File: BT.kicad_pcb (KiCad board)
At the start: 4 copper layers, 55 x 40 mm, 77 parts, among them J1 Conn_01x06_Pin, J2 Conn_01x05_Pin, J3 Conn_01x03_Pin, K1 AGQ200S12Z, Q1 BSS123, U1 ESP32-WROOM-32U, U2 AMS1117-3.3, U3 AP64060WU-7, U5 TPS7A4701, U6 PCM5100A, U7 CP2102N-A02-GQFN28, Y1 XO32

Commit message: rough placement
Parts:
- removed the C10 at (185.7, 102.7)
- removed the C25 at (205.3, 84.4)
- removed the C26 at (205.3, 86.9)
- removed the C9 at (185.7, 105.2)
- removed the R1 at (179.2, 79.2)
- removed R11, R24: 10K, NRD_RES:R_0603
- removed the R15 at (192.7, 89.7)
- removed the R16 at (192.7, 87.2)
- removed the R17 at (192.7, 84.7)
- removed the R2 at (183.4, 79.0)
- removed R21: 22K1, NRD_RES:R_0603
- removed R22: 47K5, NRD_RES:R_0603
- removed R23: 1K, NRD_RES:R_0603
- removed the R4 at (183.4, 76.5)
- removed the R5 at (179.2, 76.7)
- removed the R7 at (192.2, 78.7)
- removed the R7 at (184.7, 96.2)
- removed U7: CP2102N-A02-GQFN28, NRD_IC_COM:CP2102N
- added J5: Conn_02x03_Odd_Even, Connector_PinHeader_1.27mm:PinHeader_2x03_P1.27mm_Vertical_SMD, F.Cu at (144.6, 106.6)
- added R3: 10K, NRD_RES:R_0603, F.Cu at (131.6, 114.2)
- added R7: 10K, NRD_RES:R_0603, F.Cu at (138.4, 114.2)
- R6: renamed from R8; value 22K1 -> 1K
- R8: value 22K1 -> 10K
- moved R16 71.2 mm to (121.8, 88.3), turned to 90 degrees
- moved Y1 68.0 mm to (122.6, 91.7), turned to 0 degrees
- moved C5 65.5 mm to (122.3, 114.1)
- moved C16 64.7 mm to (123.3, 88.3), turned to 90 degrees
- moved C19 63.2 mm to (124.4, 85.1)
- moved C6 61.6 mm to (125.3, 114.1), turned to 0 degrees
- moved C26 59.2 mm to (124.7, 83.4), turned to 0 degrees
- moved R17 58.6 mm to (124.7, 81.9)
- moved C10 57.8 mm to (128.3, 114.1), turned to 0 degrees
- moved R15 55.2 mm to (124.8, 89.1), turned to 90 degrees
- moved R14 55.1 mm to (124.8, 92.0), turned to -90 degrees
- moved R6 54.9 mm to (135.1, 114.2), turned to 0 degrees
- moved R13 54.3 mm to (126.3, 92.0), turned to -90 degrees
- moved C21 54.3 mm to (133.2, 81.4), turned to 90 degrees
- moved C20 54.3 mm to (133.2, 84.8), turned to -90 degrees
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- renumbered C3 to C1, C5 to C10, C19 to C11, C13 to C12, C8 to C13, C10 to C16, C15 to C17, C17 to C18, C24 to C19, C4 to C2, C21 to C20, C23 to C21, C16 to C22, C20 to C23, C9 to C24, C14 to C25, C22 to C26, C1 to C3, C2 to C4, C11 to C5, C7 to C6, C18 to C7, C6 to C8, C12 to C9, J2 to J1, J3 to J2, J1 to J3, L2 to L1, R9 to R1, R12 to R13, R13 to R14, R14 to R15, R18 to R16, R19 to R17, R7 to R18, R20 to R19, R3 to R2, R8 to R20, R10 to R4, R6 to R5, TP3 to TP1, TP1 to TP2, TP2 to TP3, U6 to U1, U1 to U2, U3 to U4, U2 to U5, U5 to U6
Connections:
- C10 pad 1: Net-(U1-EN) -> Net-(U2-EN)
- C3 pad 1: /+3V3A_FLT -> +3.3VA
- C4 pad 1: /+3V3A_FLT -> +3.3VA
- J2 pad 1: Net-(J3-Pin_1) -> Net-(J2-Pin_1)
- R18 pad 2: Net-(U3-FB) -> Net-(U4-FB)
- R20 pad 1: Net-(U3-FB) -> Net-(U4-FB)
- R6 pad 1: Net-(U3-FB) -> Net-(J2-Pin_1)
- R6 pad 2: GND -> /LED
- R8 pad 1: Net-(U3-FB) -> /SW_TO_BT_AUDIO
- R8 pad 2: +3V3 -> GND
- S1 pad 1: Net-(U1-EN) -> unconnected-(S1-Pad1)
- S1 pad 2: Net-(U1-EN) -> unconnected-(S1-Pad2)
- S1 pad 3: GND -> unconnected-(S1-Pad3)
- S1 pad 4: GND -> unconnected-(S1-Pad4)
- U1 pad 10: Net-(U6-DEMP) -> /DAC_DMP
- U1 pad 11: Net-(U6-FLT) -> /DAC_FLT
- U1 pad 16: Net-(U6-FMT) -> /DAC_FMT
- U1 pad 8: /+3V3A_FLT -> +3.3VA
- U2 pad 10: unconnected-(U1-IO25-Pad10) -> /DAC_FMT
- U2 pad 3: Net-(U1-EN) -> Net-(U2-EN)
- U2 pad 33: unconnected-(U1-IO21-Pad33) -> /DAC_FLT
- U2 pad 36: unconnected-(U1-IO22-Pad36) -> /DAC_DMP
- U4 pad 3: Net-(U3-FB) -> Net-(U4-FB)
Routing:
- net /BCK: track 8.90 -> 0.00 mm
- net /DIN: track 10.3 -> 3.59 mm
- net /LRCK: track 8.58 -> 3.59 mm
- net /OUT_L: track 8.92 -> 12.0 mm
- net /OUT_R: track 9.96 -> 13.0 mm
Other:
- board text removed: "6B - BangBoomBlauzahnBlaupunktBassBox Rev. A"

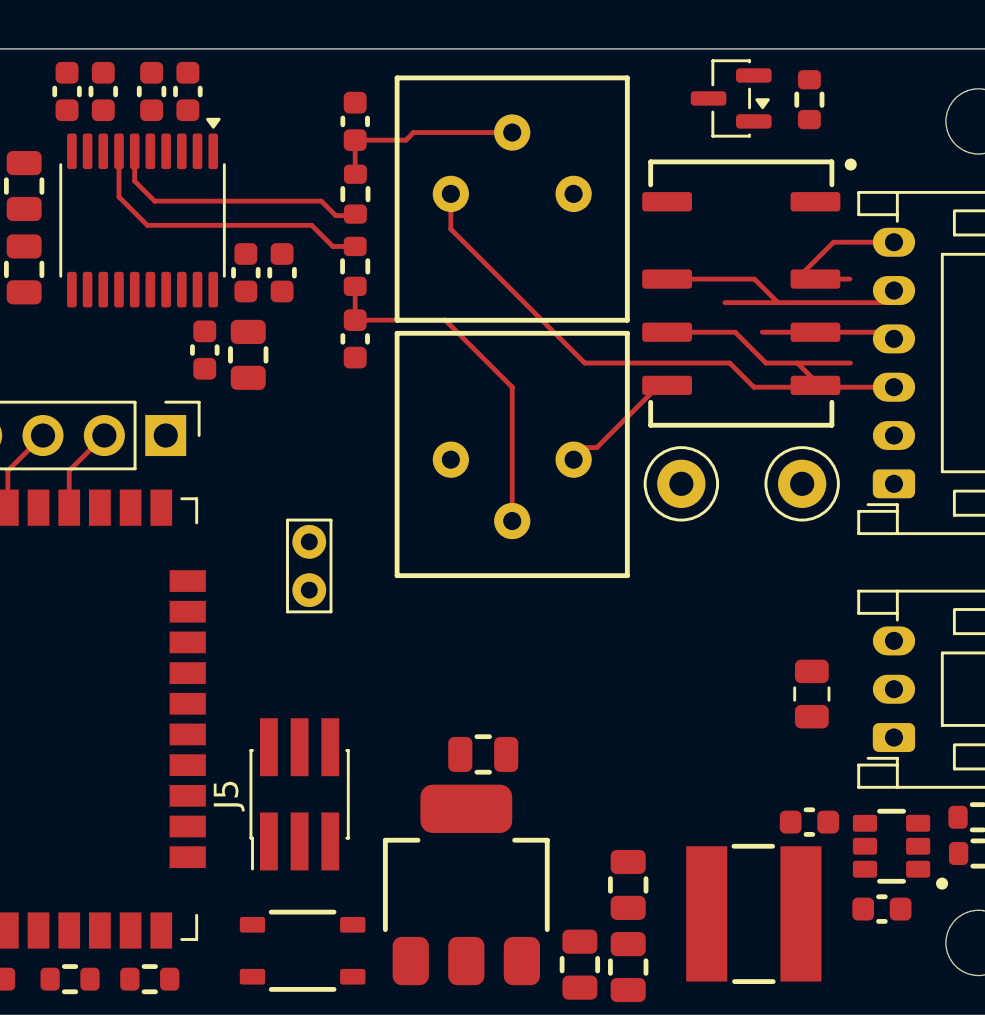
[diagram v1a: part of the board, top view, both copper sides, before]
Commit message: added amplifier. So control volume by knob, signal has to be in injected before the volume control poti. This is why around 5V signal amplitude are necessary.
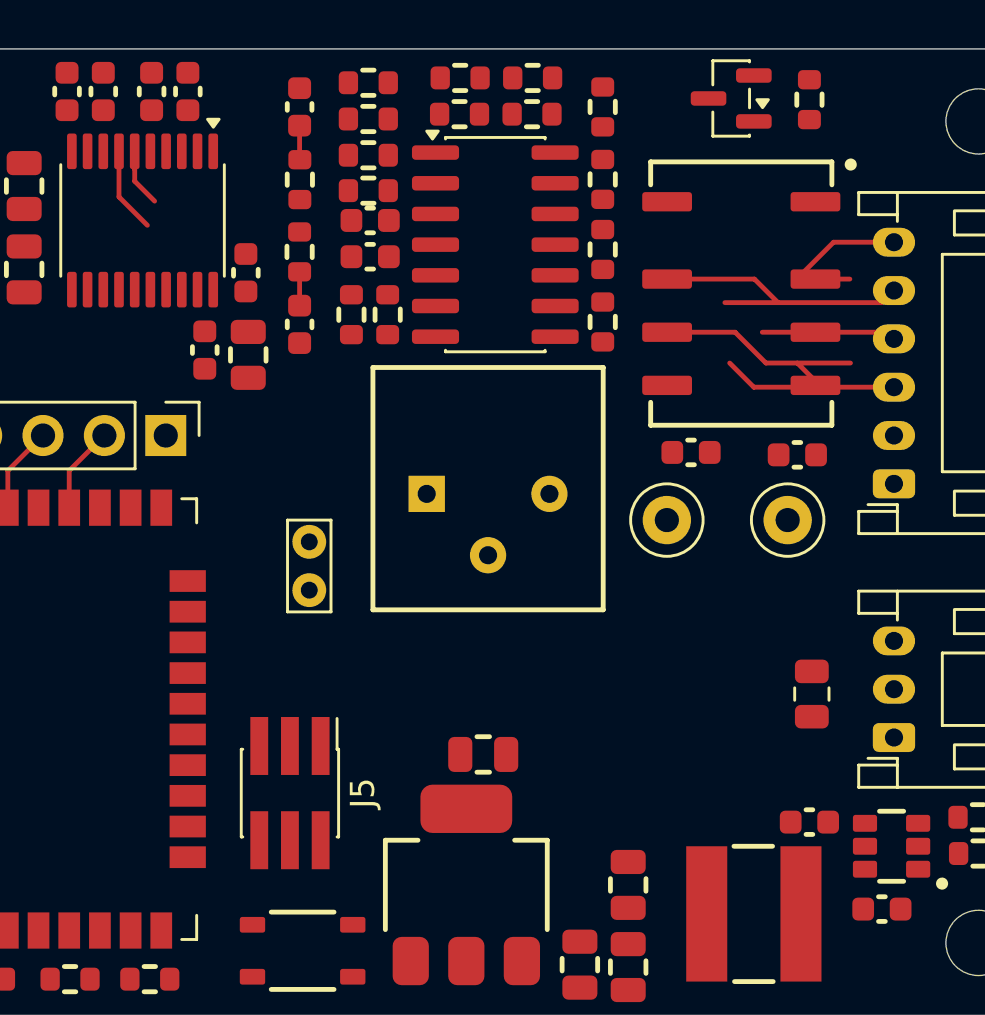
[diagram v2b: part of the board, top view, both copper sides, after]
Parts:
- removed C2: 100nF, NRD_CAP:C_0603
- removed R5: 10K, NRD_R_Var:3296P
- added C14: 220nF, NRD_CAP:C_0603, F.Cu at (165.2, 92.5)
- added C15: 220nF, NRD_CAP:C_0603, F.Cu at (160.8, 92.4)
- added C27: 10nF, NRD_CAP:C_0603, F.Cu at (147.5, 84.3)
- added C28: 100nF, NRD_CAP:C_0603, F.Cu at (147.5, 82.8)
- added R10: 1M, NRD_RES:R_0603, F.Cu at (147.4, 81.6)
- added R11: 1M, NRD_RES:R_0603, F.Cu at (151.2, 76.9)
- added R12: 1M, NRD_RES:R_0603, F.Cu at (147.4, 77.1)
- added R21: 10K, NRD_RES:R_0603, F.Cu at (147.4, 78.6)
- added R22: 1M, NRD_RES:R_0603, F.Cu at (146.7, 86.7)
- added R23: 1M, NRD_RES:R_0603, F.Cu at (154.2, 76.9)
- added R24: 1M, NRD_RES:R_0603, F.Cu at (148.2, 86.7)
- added R25: 1M, NRD_RES:R_0603, F.Cu at (157.1, 78.1)
- added R26: 10K, NRD_RES:R_0603, F.Cu at (157.1, 87.0)
- added R27: 1M, NRD_RES:R_0603, F.Cu at (151.2, 78.4)
- added R28: 1M, NRD_RES:R_0603, F.Cu at (154.2, 78.4)
- added R29: 1M, NRD_RES:R_0603, F.Cu at (157.1, 84.0)
- added R30: 1M, NRD_RES:R_0603, F.Cu at (157.1, 81.1)
- added R9: 1M, NRD_RES:R_0603, F.Cu at (147.4, 80.1)
- added U3: TL084, Package_SO:SOIC-14_3.9x8.7mm_P1.27mm, F.Cu at (152.7, 83.8)
- moved R2 12.5 mm to (152.4, 94.1), turned to 90 degrees
- moved R1 2.38 mm to (144.6, 81.1)
- moved C8 2.38 mm to (144.6, 87.1)
- moved C9 2.38 mm to (144.6, 78.1)
- moved R4 2.38 mm to (144.6, 84.1)
- moved TP2 1.62 mm to (164.8, 95.2)
- moved TP3 1.62 mm to (159.8, 95.2)
- moved J5 0.40 mm to (144.2, 106.5), turned to -90 degrees
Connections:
- C10 pad 1: Net-(U2-EN) -> /ESP_EN
- J5 pad 1: unconnected-(J5-Pin_1-Pad1) -> /ESP_EN
- J5 pad 2: unconnected-(J5-Pin_2-Pad2) -> +3V3
- J5 pad 3: unconnected-(J5-Pin_3-Pad3) -> /ESP_TXD0
- J5 pad 4: unconnected-(J5-Pin_4-Pad4) -> GND
- J5 pad 5: unconnected-(J5-Pin_5-Pad5) -> /ESP_RXD0
- J5 pad 6: unconnected-(J5-Pin_6-Pad6) -> /ESP_IO0
- R2 pad 1: unconnected-(R2-Pad1) -> Net-(C14-Pad2)
- R2 pad 2: Net-(C9-Pad1) -> GND
- R2 pad 3: /OUT_L_CON -> Net-(R2-Pad3)
- R3 pad 2: Net-(U2-EN) -> /ESP_EN
- S1 pad 1: unconnected-(S1-Pad1) -> /ESP_EN
- S1 pad 2: unconnected-(S1-Pad2) -> /ESP_EN
- S1 pad 3: unconnected-(S1-Pad3) -> GND
- S1 pad 4: unconnected-(S1-Pad4) -> GND
- TP2 pad 1: /OUT_L_CON -> Net-(C14-Pad2)
- TP3 pad 1: /OUT_R_CON -> Net-(C15-Pad2)
- U2 pad 25: unconnected-(U2-IO0-Pad25) -> /ESP_IO0
- U2 pad 27: /BCK -> /MCLK
- U2 pad 28: /LRCK -> /BCK
- U2 pad 3: Net-(U2-EN) -> /ESP_EN
- U2 pad 30: /DIN -> /LRCK
- U2 pad 31: unconnected-(U2-IO19-Pad31) -> /DIN
- U2 pad 34: /MCLK -> /ESP_RXD0
- U2 pad 35: unconnected-(U2-TXD0/IO1-Pad35) -> /ESP_TXD0
- U6 pad 17: (no net) -> unconnected-(U6-NC-Pad17)
- U6 pad 18: (no net) -> unconnected-(U6-NC-Pad18)
- U6 pad 19: (no net) -> unconnected-(U6-NC-Pad19)
- U6 pad 2: (no net) -> unconnected-(U6-NC-Pad2)
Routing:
- net /OUT_L_CON: track 19.3 -> 4.00 mm
- net Net-(C8-Pad1): track 14.6 -> 1.40 mm
- net /OUT_R: track 13.0 -> 4.05 mm
- net /OUT_L: track 12.0 -> 3.44 mm
- net Net-(C9-Pad1): track 8.04 -> 1.41 mm
- net /OUT_R_CON: track 4.94 -> 0.34 mm

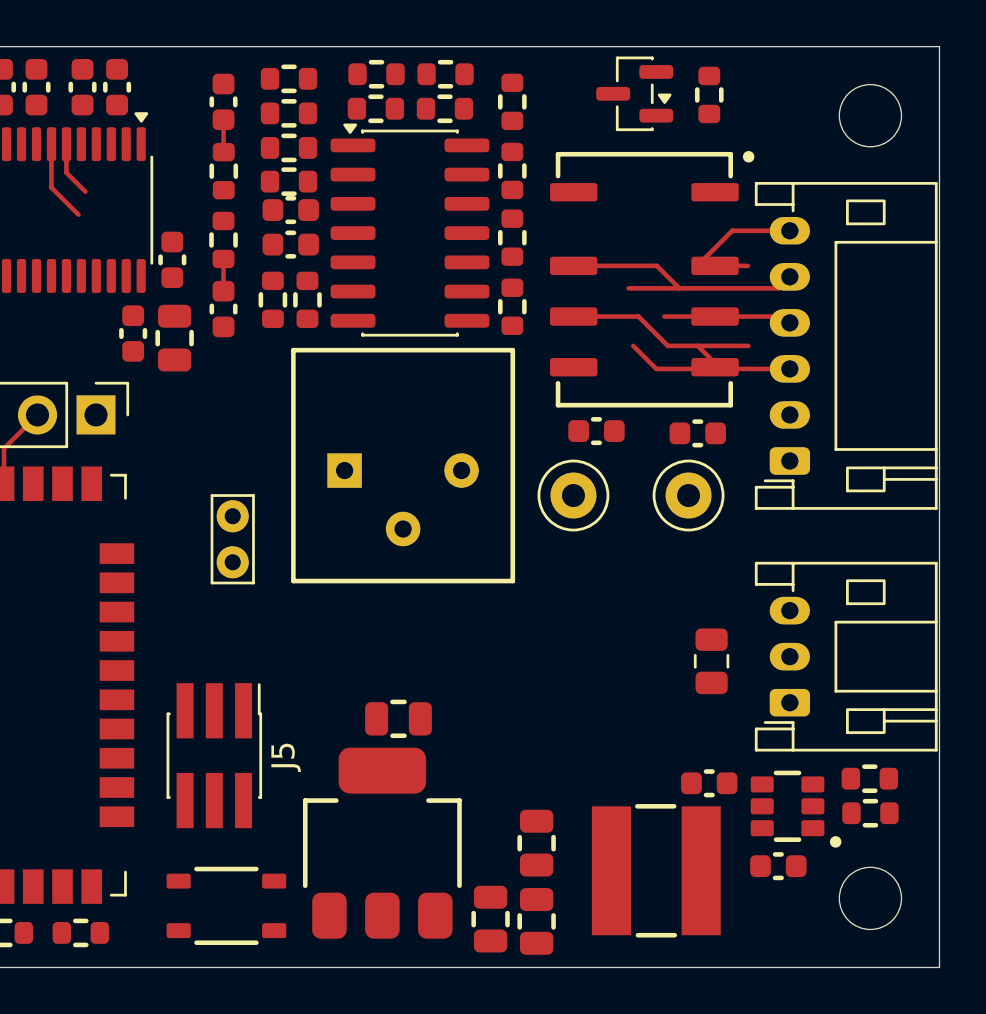
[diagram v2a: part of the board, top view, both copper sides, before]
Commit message: Increased intermediate rail from 5 to 6V; replaced LDO for diigital supply by DCDC
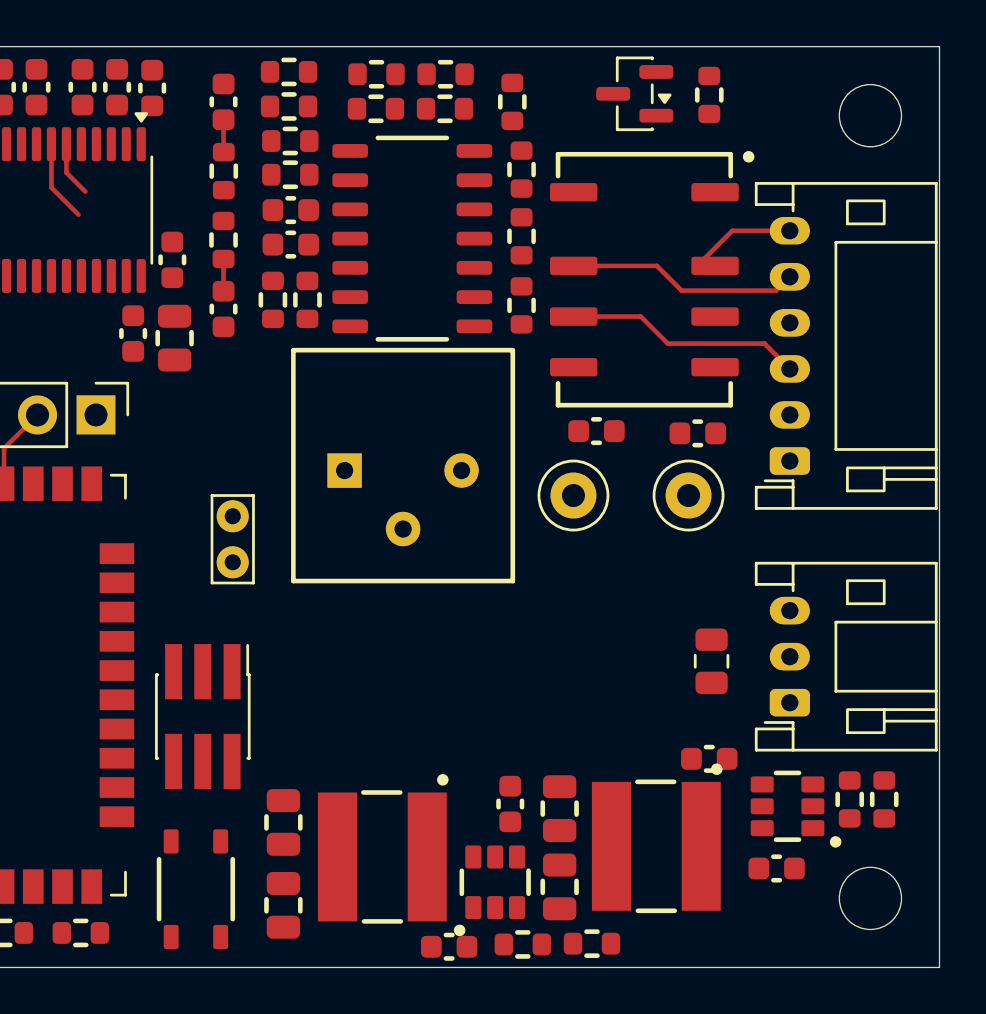
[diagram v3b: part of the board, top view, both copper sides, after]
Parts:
- removed C22, C23: 22uF, NRD_CAP:C_0805
- removed U5: AMS1117-3.3, NRD_LDO:AMS1117
- added C2: 100nF, NRD_CAP:C_0603, F.Cu at (141.5, 77.5)
- added C29: 2.2uF, NRD_CAP:C_0603, F.Cu at (157.0, 108.6)
- added C30: 100nF, NRD_CAP:C_0603, F.Cu at (154.4, 114.8)
- added C31: 10uF, NRD_CAP:C_0805, F.Cu at (147.2, 113.0)
- added C32: 10uF, NRD_CAP:C_0805, F.Cu at (147.2, 109.4)
- added L2: 8.2uH, NRD_IND:74438367082, F.Cu at (151.5, 110.9)
- added R31: 11K5, NRD_RES:R_0603, F.Cu at (160.6, 114.7)
- added R5: 13K, NRD_RES:R_0603, F.Cu at (173.3, 108.4)
- added U7: AP64060WU-7, NRD_IC_DCDC:AP6406x, F.Cu at (156.4, 112.0)
- R18: value 115K -> 2K
- R20: value 22K1 -> 35K7
- U3: value TL084 -> TLV4888DR; footprint Package_SO:SOIC-14_3.9x8.7mm_P1.27mm -> NRD_IC_OPAMP:TLV4888DR
- moved R20 16.7 mm to (157.6, 114.7), turned to 0 degrees
- moved C24 1.80 mm to (159.2, 112.2)
- moved C25 1.80 mm to (159.2, 108.8)
- moved J5 1.77 mm to (143.7, 104.8)
- moved S1 1.51 mm to (143.4, 112.3), turned to -90 degrees
- moved R18 1.08 mm to (171.8, 108.4), turned to -90 degrees
- moved C18 1.06 mm to (165.7, 106.6)
- moved L1 1.06 mm to (163.4, 110.4)
- moved R26 0.40 mm to (157.5, 87.0)
- moved R29 0.40 mm to (157.5, 84.0)
- moved R30 0.40 mm to (157.5, 81.0)
- moved R10 0.30 mm to (147.5, 81.3)
- moved R9 0.30 mm to (147.5, 79.8)
- moved R12 0.30 mm to (147.4, 76.8)
- moved R21 0.30 mm to (147.4, 78.3)
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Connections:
- net Net-(U4-BST) renamed /BST_+6V
- C24 pad 1: +5V -> +6V
- C25 pad 1: +5V -> +6V
- L1 pad 2: +5V -> +6V
- R18 pad 1: +5V -> /FB_+6V
- R18 pad 2: Net-(U4-FB) -> GND
- R20 pad 1: Net-(U4-FB) -> +3V3
- R20 pad 2: GND -> /FB_+3V3
- R27 pad 1: Net-(U3D--) -> Net-(U3C-+)
- R28 pad 2: Net-(U3D--) -> Net-(U3C-+)
- R29 pad 1: Net-(U3D-+) -> Net-(U3C--)
- R30 pad 2: Net-(U3D-+) -> Net-(U3C--)
- U3 pad 10: unconnected-(U3C-+-Pad10) -> Net-(U3C-+)
- U3 pad 12: Net-(U3D-+) -> unconnected-(U3D-+-Pad12)
- U3 pad 13: Net-(U3D--) -> unconnected-(U3D---Pad13)
- U3 pad 14: Net-(C15-Pad2) -> unconnected-(U3-Pad14)
- U3 pad 8: unconnected-(U3-Pad8) -> Net-(C15-Pad2)
- U3 pad 9: unconnected-(U3C---Pad9) -> Net-(U3C--)
- U4 pad 3: Net-(U4-FB) -> /FB_+6V
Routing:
- net /L_OUT: track 5.56 -> 0.39 mm
- net /OUT_L_CON: track 4.00 -> 0.11 mm
- net /R_OUT: track 12.5 -> 10.3 mm
- net /R_IN: track 12.2 -> 10.1 mm
- net /L_IN: track 6.08 -> 4.66 mm
